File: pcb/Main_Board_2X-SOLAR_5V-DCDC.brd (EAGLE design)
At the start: 77.1 x 38.9 mm, 72 parts, among them CN5 USBA_FEMALE, M3AB FDMC8030, M4 SI7611DN, M5 FDMC8327L, T2 MMUN2133LT1G, U1 LTC4015EUHFPBFQFN-38_UHF-M, U3 TPS61090RSAR, X1 6V_PV

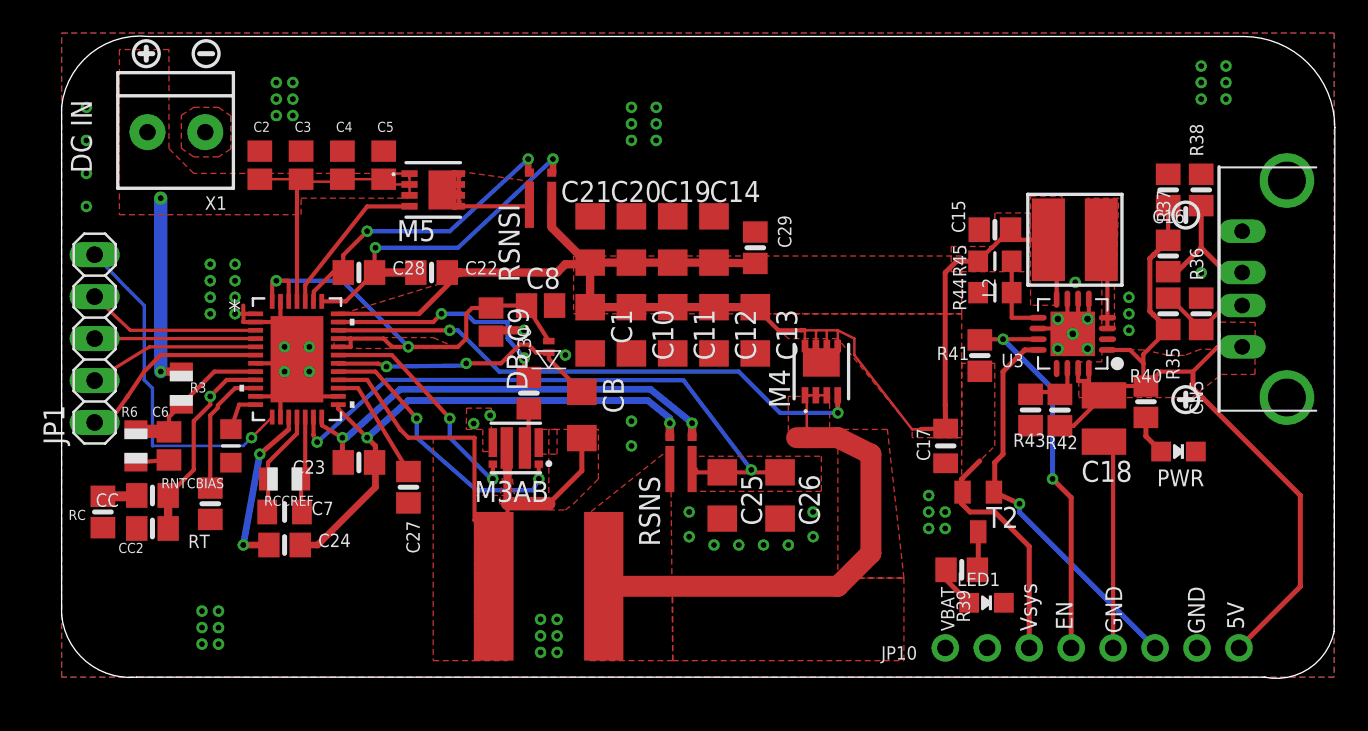
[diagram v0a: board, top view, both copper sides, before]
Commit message: OSH V1 print board and schematic update
Finalized routings for signal and power. Updated silkscreen text for clarity during assembly.
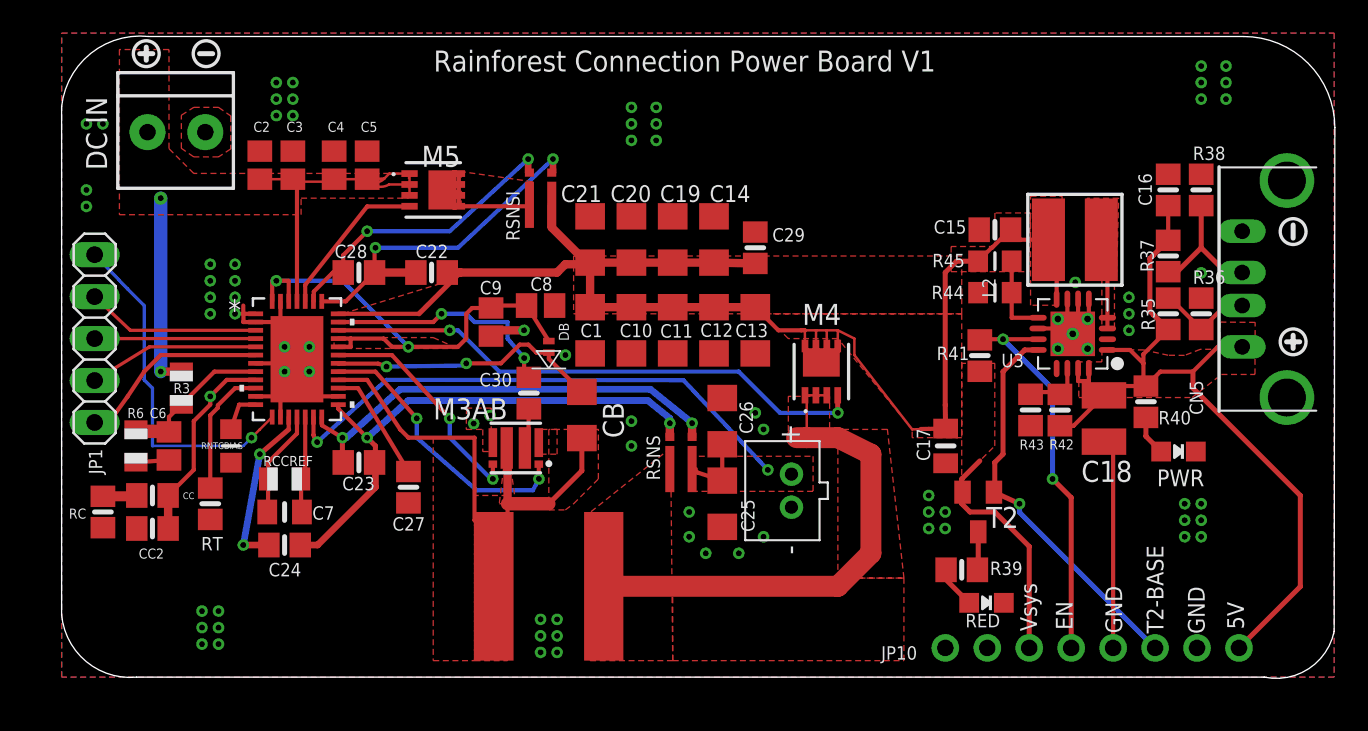
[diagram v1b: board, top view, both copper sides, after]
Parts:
- added CN1: (no value), adafruit:JST-PH-2-THM
- moved U$86 7.38 mm to (74.6, 20.3)
- moved U$87 6.58 mm to (74.6, 27.0)
- moved C26 5.70 mm to (40.0, 15.5), turned to 90 degrees
- moved C5 1.00 mm to (18.5, 31.0)
- moved C25 0.50 mm to (40.0, 10.5)
- moved C3 0.50 mm to (14.0, 31.0)
- moved C4 0.50 mm to (16.5, 31.0)
- renumbered LED1 to RED
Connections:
- net BAT: now also CN1.1
- net GND: now also CN1.2
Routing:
- net VIN: track 31.7 -> 34.1 mm
- net BAT: track 37.7 -> 37.1 mm
- net GND: vias 64 -> 75
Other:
- board text added: "2.7V Low Batt Indicator"
- board text added: "Rainforest Connection Power Board V1"
- board text added: "T2-BASE"
- board text removed: "3.2V Low Batt Indicator"
- board text removed: "LiPoly 3.7-4.2 V only!"
- board text removed: "USB: 1A Charge Rate"
- board text removed: "VBAT"
- board text removed: "Vsh: larger of USB/LiPo"
- board text removed: "iOS 1A Charge Resistors"

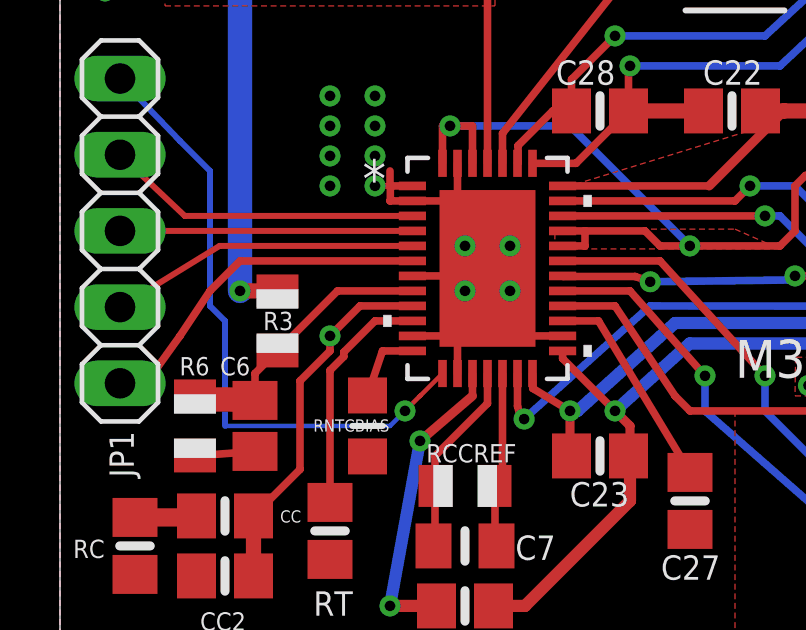
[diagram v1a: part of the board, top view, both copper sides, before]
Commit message: Updated schematic with UVCLFB input
added 10k resistor
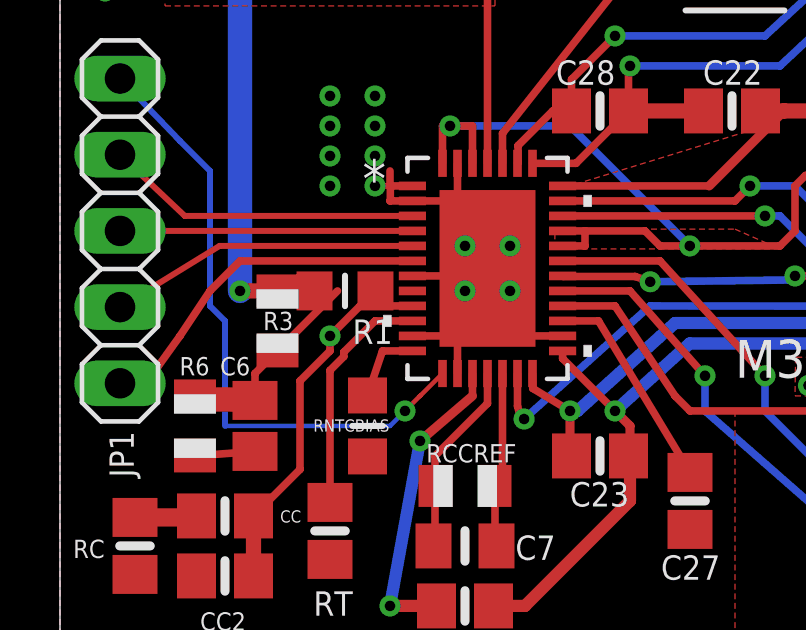
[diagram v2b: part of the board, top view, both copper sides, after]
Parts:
- added R1: 10k, microbuilder:_0805MP
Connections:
- new net N$5: R1.1, U1.8
- net UVCLFB: now also R1.2; no longer U1.8
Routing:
- net UVCLFB: track 9.34 -> 6.84 mm
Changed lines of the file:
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@@
 </element>
 <element name="CN1" library="adafruit" library_urn="urn:adsk.eagle:library:420" package="JST-PH-2-THM" value="" x="44.19" y="11.29" smashed="yes" rot="R90"/>
+<element name="R1" library="microbuilder" package="_0805MP" value="10k" x="9.5" y="18.5" rot="R180"/>
 </elements>
 <signals>
@@
 <signal name="UVCLFB">
 <contactref element="C6" pad="1"/>
-<contactref element="U1" pad="8"/>
 <contactref element="R6" pad="2"/>
 <contactref element="R3" pad="1"/>
 <wire x1="4.5" y1="15" x2="4.625" y2="14.875" width="0.3048" layer="1"/>
 <wire x1="4.625" y1="14.875" x2="6.5" y2="14.85" width="0.8128" layer="1" curve="-5.349506"/>
-<wire x1="11.7468" y1="18.5" x2="9.25" y2="18.5" width="0.254" layer="1"/>
 <wire x1="7.25" y1="16.5" x2="9.25" y2="18.5" width="0.254" layer="1"/>
 <wire x1="6.5" y1="14.85" x2="6.5" y2="15.75" width="0.254" layer="1"/>
 <wire x1="6.5" y1="15.75" x2="7.25" y2="16.5" width="0.254" layer="1"/>
+<contactref element="R1" pad="2"/>
+<wire x1="4.5" y1="15" x2="8.484" y2="18.5" width="0" layer="19" extent="1-1"/>
 </signal>
 <signal name="VIN">
@@
 <wire x1="53.55" y1="5.9" x2="54.95" y2="4.5" width="0.3048" layer="1"/>
 </signal>
+<signal name="N$5">
+<contactref element="R1" pad="1"/>
+<contactref element="U1" pad="8"/>
+<wire x1="10.516" y1="18.5" x2="11.7468" y2="18.5" width="0" layer="19" extent="1-1"/>
+</signal>
 </signals>

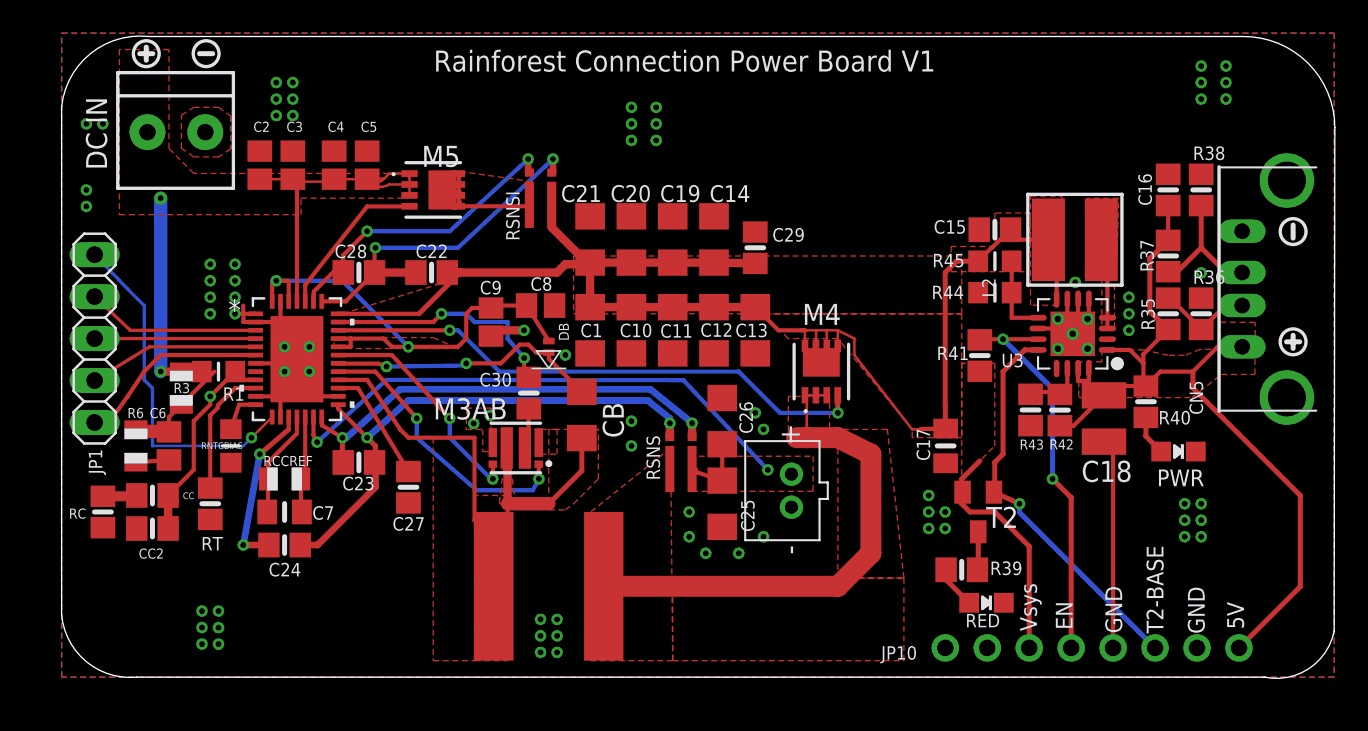
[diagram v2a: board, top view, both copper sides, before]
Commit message: Updates to schematic and board layout to fix V1
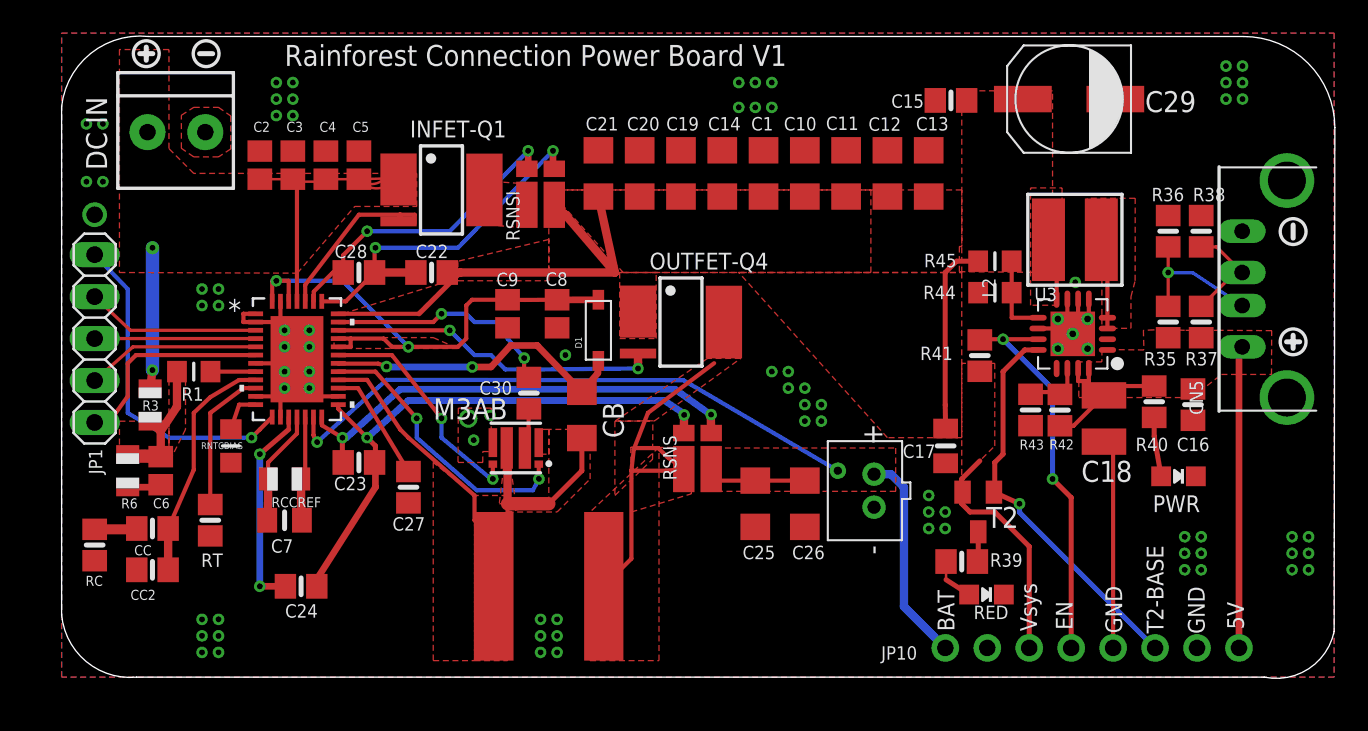
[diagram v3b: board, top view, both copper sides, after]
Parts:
- removed DB: 1N4448HLP, RCT:DO214AC
- removed M4: SI7611DN, Si7611DN:POWERPAK_1212_8
- removed M5: FDMC8327L, RCT:8-POWER_W_DFN
- added D1: (no value), adafruit:SOD-123
- added INFET-Q1: SI4840DY, TRANS_SI7635DP-T1-GE3:SO08-E3
- added OUTFET-Q4: SQ4401EY-PMOS, TRANS_SI7635DP-T1-GE3:SO08-E3
- C29: value 120 uF -> NICHICON-RSA-AL-POLY-CAP; device microbuilder:0805-NO -> RCT:RSA-CAP-SMD
- moved C29 21.0 mm to (61.0, 35.0), turned to 90 degrees
- moved C1 14.2 mm to (42.5, 30.5), turned to 90 degrees
- moved C10 14.2 mm to (45.0, 30.5), turned to 90 degrees
- moved C11 14.2 mm to (47.5, 30.5), turned to 90 degrees
- moved C12 14.2 mm to (50.0, 30.5), turned to 90 degrees
- moved C13 14.2 mm to (52.5, 30.5), turned to 90 degrees
- moved C16 13.1 mm to (68.5, 16.5), turned to 270 degrees
- moved C15 8.27 mm to (53.8, 34.9)
- moved C26 7.07 mm to (45.0, 10.5), turned to 270 degrees
- moved R36 5.39 mm to (67.0, 27.0)
- moved CN1 5.00 mm to (49.2, 11.3)
- moved R37 4.47 mm to (69.0, 21.5), turned to 270 degrees
- moved C14 4.03 mm to (40.0, 30.5)
- moved C19 4.03 mm to (37.5, 30.5)
- moved C20 4.03 mm to (35.0, 30.5)
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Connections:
- removed net OUTFET: M4.4, U1.29
- removed net VBUS: JP10.1
- new net N$10: OUTFET-Q4.4, U1.29
- net BAT: now also JP10.1
- net GND: now also C29.P$1, JP10.2; no longer C29.1
- net INFET: now also INFET-Q1.4; no longer M5.4
- net INTVCC: now also D1.A; no longer DB.A
- net N$13: now also D1.C; no longer DB.C
- net N$3: now also INFET-Q1.5-8; no longer M5.10, M5.5, M5.6, M5.7, M5.8
- net OUTFET_M4_SOURCE: now also OUTFET-Q4.5-8; no longer M4.1, M4.2, M4.3
- net SYS: now also C29.P$2, OUTFET-Q4.1-3; no longer C29.2, M4.5, M4.6, M4.7, M4.8
- net VIN: now also INFET-Q1.1-3; no longer M5.1, M5.2, M5.3
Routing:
- net SYS: track 100.0 -> 59.0 mm
- net OUTFET: track 33.4 -> 0.00 mm, vias 2 -> 0
- net 5.0V: track 53.0 -> 29.0 mm
- net N$10: track 0.00 -> 20.0 mm, vias 0 -> 2
- net BAT: track 37.1 -> 55.3 mm
- net OUTFET_M4_SOURCE: track 31.7 -> 23.1 mm
- net N$3: track 7.42 -> 0.11 mm
- net VIN: track 34.1 -> 29.1 mm
- net GND: track 45.9 -> 42.8 mm, vias 75 -> 77
- net D-1: track 5.87 -> 8.89 mm, vias 0 -> 1
- net N$5: track 0.00 -> 2.73 mm
- net INTVCC: track 30.4 -> 33.0 mm
- net CSPM5: track 10.2 -> 12.6 mm
- net SW_LTC: track 33.8 -> 31.6 mm
- net N$13: track 16.8 -> 18.8 mm
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- added copper zone on layer 1, net UVCLFB
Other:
- board text added: "BAT"
- board text added: "SYS"
- board text removed: "Vbat"
